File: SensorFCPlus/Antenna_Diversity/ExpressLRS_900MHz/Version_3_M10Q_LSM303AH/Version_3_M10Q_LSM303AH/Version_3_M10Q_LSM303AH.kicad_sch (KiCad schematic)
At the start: 37 parts, among them J1 Conn_01x05_Pin, J2 Conn_01x02_Pin, J3 Conn_01x05_Pin, J4 Conn_01x03_Pin, U1 LSM303AHTR, U2 SAM-M10Q-00B, U3 BAT54STA, U4 TPS7A4701xRGW, U7 U.FL-R-SMT, U8 U.FL-R-SMT

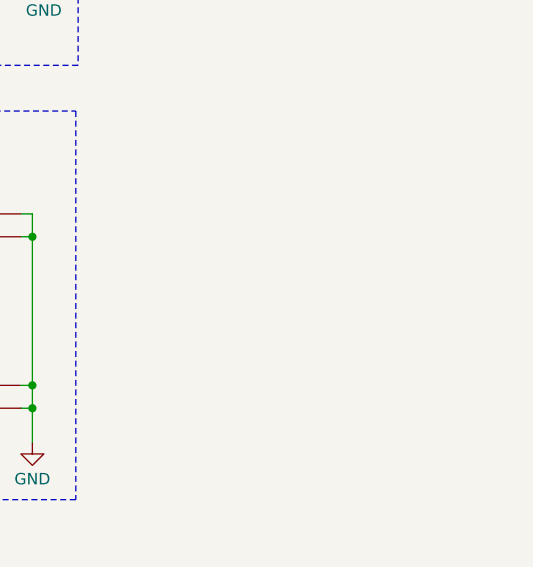
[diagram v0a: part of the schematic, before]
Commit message: Update KiCad files for ExpressLRS modules
- Modified:
  - 2.4GHz Version 3 (M10Q LSM303AH) project and schematic files
  - 900MHz Version 3 (M10Q LSM303AH) schematic files for ESP8285 and SE2435L

- Added:
  - 2.4GHz Version 3 schematics: ESP8285, SE2431, SE2431L, SX1280
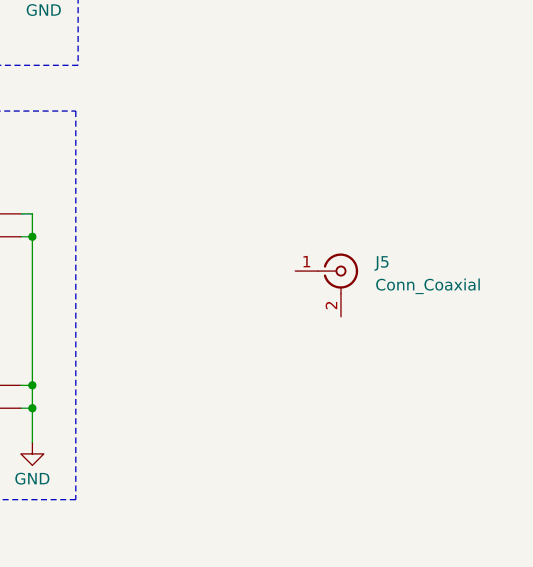
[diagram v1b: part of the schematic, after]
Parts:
- added J5: Conn_Coaxial, Connector_Coaxial:U.FL_Hirose_U.FL-R-SMT-1_Vertical, symbol Connector:Conn_Coaxial
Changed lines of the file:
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@@
+	)
+	(symbol
+		(lib_id "Connector:Conn_Coaxial")
+		(at 309.88 135.89 0)
+		(unit 1)
+		(exclude_from_sim no)
+		(in_bom yes)
+		(on_board yes)
+		(dnp no)
+		(fields_autoplaced yes)
+		(property "Reference" "J5"
+			(at 313.69 134.9131 0)
+			(effects
+				(font
+					(size 1.27 1.27)
+				)
+				(justify left)
+			)
+		)
+		(property "Value" "Conn_Coaxial"
+			(at 313.69 137.4531 0)
+			(effects
+				(font
+					(size 1.27 1.27)
+				)
+				(justify left)
+			)
+		)
+		(property "Footprint" "Connector_Coaxial:U.FL_Hirose_U.FL-R-SMT-1_Vertical"
+			(at 309.88 135.89 0)
+			(effects
+				(font
+					(size 1.27 1.27)
+				)
+				(hide yes)
+			)
+		)
+		(property "Datasheet" "~"
+			(at 309.88 135.89 0)
+			(effects
+				(font
+					(size 1.27 1.27)
+				)
+				(hide yes)
+			)
+		)
+		(property "Description" "coaxial connector (BNC, SMA, SMB, SMC, Cinch/RCA, LEMO, ...)"
+			(at 309.88 135.89 0)
+			(effects
+				(font
+					(size 1.27 1.27)
+				)
+				(hide yes)
+			)
+		)
+		(pin "1"
+		)
+		(pin "2"
+		)
+		(instances
+			(project ""
+				(path "/c831470d-4a3e-4c64-b711-9d439212075e"
+					(reference "J5")
+					(unit 1)
+				)
+			)
+		)
 	)
 	(symbol
